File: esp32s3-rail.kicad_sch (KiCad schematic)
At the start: 42 parts, among them J1 RJ45_Wuerth_7499010121A, J2 WR-WST 490107670412, Q1 AO3407A, U1 ESP32-S3-MINI-1U, U2 W5500, U3 THVD1420D, Y1 25M

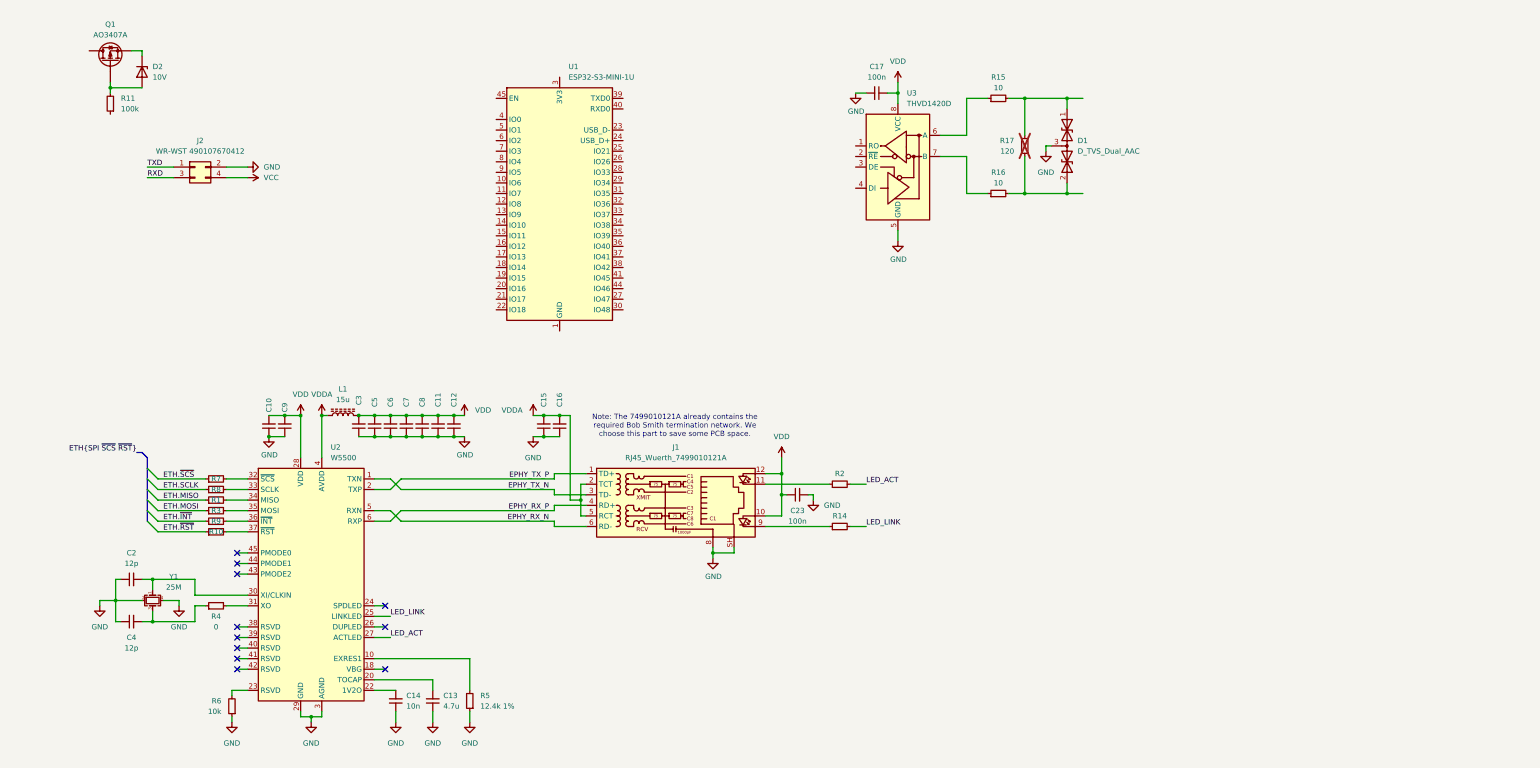
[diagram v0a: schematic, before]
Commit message: Update schematic: - Add RS485 ports - Add USB ports - Add 24V I/O ports
Signed-off-by: Dominik Bayerl <dominik.bayerl@carissma.eu>
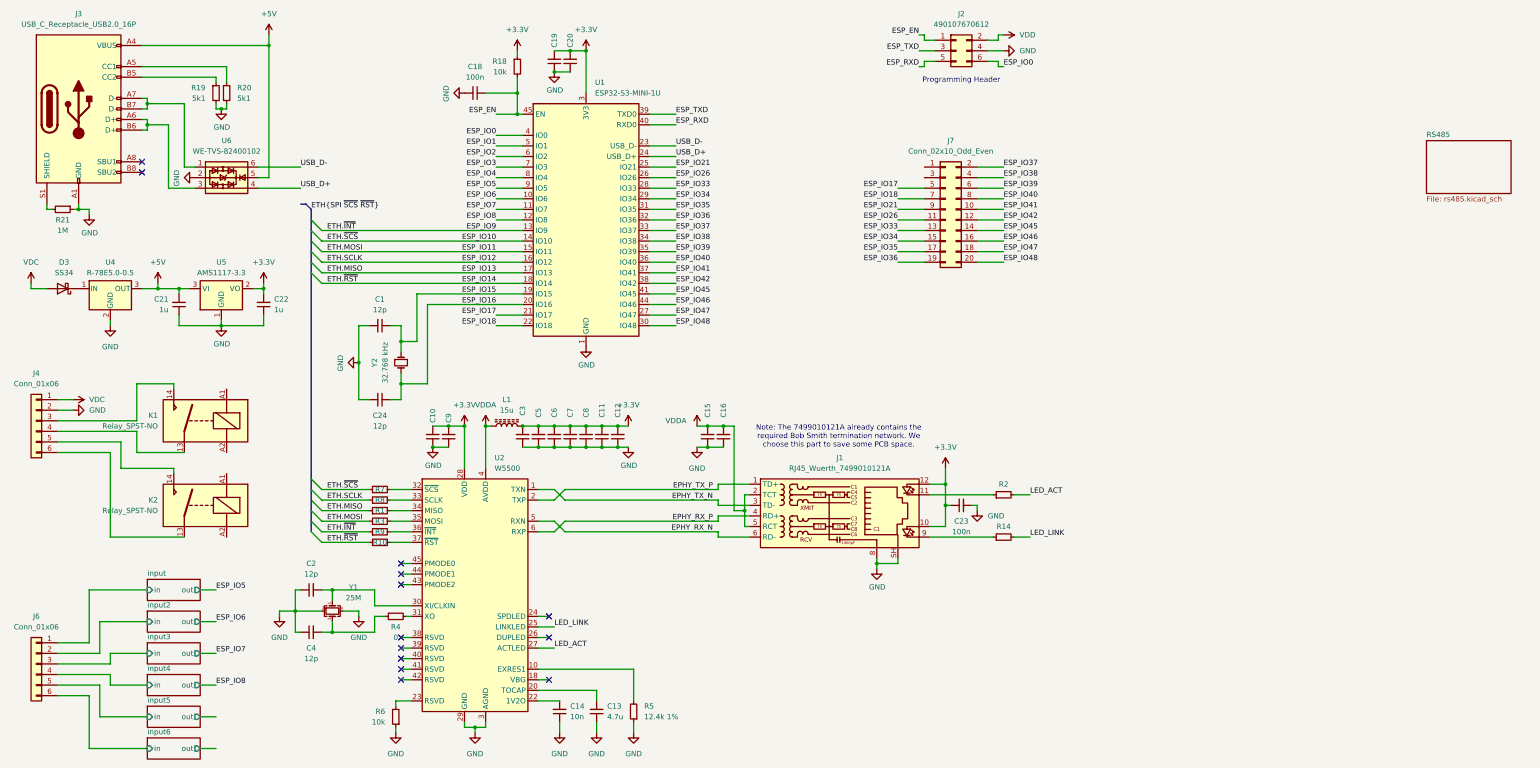
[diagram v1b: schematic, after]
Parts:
- removed C17: 100n, symbol Device:C_Small
- removed D1: D_TVS_Dual_AAC, Package_TO_SOT_SMD:SOT-23, symbol Device:D_TVS_Dual_AAC
- removed D2: 10V, symbol Device:D_Zener
- removed J2: WR-WST 490107670412, Connector_Wuerth_WST:Würth_WR-WST_debug_490107670412_2x02_P2.54mm_Vertical, symbol Connector_Generic:Conn_02x02_Odd_Even
- removed Q1: AO3407A, Package_TO_SOT_SMD:SOT-23, symbol Device:Q_PMOS
- removed R11: 100k, Resistor_SMD:R_0603_1608Metric, symbol Device:R_Small
- removed R15, R16: 10, Resistor_SMD:R_1206_3216Metric, symbol Device:R_Small
- removed R17: 120, Resistor_SMD:R_1206_3216Metric, symbol Device:R_Small
- removed U3: THVD1420D, Package_SO:SOIC-8_3.9x4.9mm_P1.27mm, symbol Interface_UART:THVD1420D
- added C1, C24: 12p, symbol Device:C_Small
- added C18: 100n, symbol Device:C_Small
- added C19, C20, C21, C22: 1u, symbol Device:C_Small
- added D3: SS34, symbol Device:D_Schottky
- added J2: 490107670612, Connector_Wuerth_WST:Würth_WR-WST_debug_490107670612_2x03_P2.54mm_Vertical, symbol Connector_Generic:Conn_02x03_Odd_Even
- added J3: USB_C_Receptacle_USB2.0_16P, symbol Connector:USB_C_Receptacle_USB2.0_16P
- added J4, J6: Conn_01x06, symbol Connector_Generic:Conn_01x06
- added J7: Conn_02x10_Odd_Even, symbol Connector_Generic:Conn_02x10_Odd_Even
- added K1, K2: Relay_SPST-NO, symbol Relay:Relay_SPST-NO
- added R18: 10k, Resistor_SMD:R_1206_3216Metric, symbol Device:R_Small
- added R19, R20: 5k1, Resistor_SMD:R_1206_3216Metric, symbol Device:R_Small
- added R21: 1M, Resistor_SMD:R_1206_3216Metric, symbol Device:R_Small
- added U4: R-78E5.0-0.5, Converter_DCDC:Converter_DCDC_RECOM_R-78E-0.5_THT, symbol Regulator_Switching:R-78E5.0-0.5
- added U5: AMS1117-3.3, Package_TO_SOT_SMD:SOT-223-3_TabPin2, symbol Regulator_Linear:AMS1117-3.3
- added U6: WE-TVS-82400102, Package_TO_SOT_SMD:SOT-23-6, symbol Power_Protection:WE-TVS-82400102
- added Y2: 32.768 kHz, Crystal:Crystal_SMD_EuroQuartz_EQ161-2Pin_3.2x1.5mm_HandSoldering, symbol Device:Crystal_Small
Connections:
- net ETH.MISO is gone; now on net ESP_IO13: R1.1
- net ETH.MOSI is gone; now on net ESP_IO11: R3.1
- net ETH.SCLK is gone; now on net ESP_IO12: R8.1
- net ETH.~{INT} is gone; now on net ESP_IO9: R9.1
- net ETH.~{RST} is gone; now on net ESP_IO14: R10.1
- net ETH.~{SCS} is gone; now on net ESP_IO10: R7.1
- net GND: now also U1.1 (GND), U1.2 (GND), U1.42 (GND), U1.43 (GND), U1.46 (GND), U1.47 (GND), U1.48 (GND), U1.49 (GND), U1.50 (GND), U1.51 (GND), U1.52 (GND), U1.53 (GND), U1.54 (GND), U1.55 (GND), U1.56 (GND), U1.57 (GND), U1.58 (GND), U1.59 (GND), U1.60 (GND), U1.61 (GND), U1.62 (GND), U1.63 (GND), U1.64 (GND), U1.65 (GND), C1.2, C18.2, C19.1, C20.1, C21.1, C22.1, C24.2, J2.4 (Pin_4), J3.A1 (GND), J3.A12 (GND), J3.B1 (GND), J3.B12 (GND), J4.2 (Pin_2), R19.2, R20.2, R21.1, U4.2 (GND), U5.1 (GND), U6.2
- net VDD: now also J2.2 (Pin_2); no longer C10.2, C11.2, C12.2, C23.1, C3.2, C5.2, C6.2, C7.2, C8.2, C9.2, J1.10, J1.12, L1.2, U2.28 (VDD)
- net ESP_IO6: now reaches U1.10 (IO6)
- net ESP_IO7: now reaches U1.11 (IO7)
- net ESP_IO8: now reaches U1.12 (IO8)
- net ESP_IO9: now reaches U1.13 (IO9)
- net ESP_IO10: now reaches U1.14 (IO10)
- net ESP_IO11: now reaches U1.15 (IO11)
- net ESP_IO12: now reaches U1.16 (IO12)
- net ESP_IO13: now reaches U1.17 (IO13)
- net ESP_IO14: now reaches U1.18 (IO14)
- net ESP_IO15: now reaches U1.19 (IO15)
- net ESP_IO15: now also C1.1, Y2.1
- net ESP_IO16: now reaches U1.20 (IO16)
- net ESP_IO16: now also C24.1, Y2.2
- net ESP_IO17: now reaches U1.21 (IO17)
- net ESP_IO17: now also J7.5 (Pin_5)
- net ESP_IO18: now reaches U1.22 (IO18)
- net ESP_IO18: now also J7.7 (Pin_7)
- net USB_D-: now reaches U1.23 (USB_D-)
- net USB_D-: now also U6.6
- net USB_D+: now reaches U1.24 (USB_D+)
- net USB_D+: now also U6.4
- net ESP_IO21: now reaches U1.25 (IO21)
- net ESP_IO21: now also J7.9 (Pin_9)
- net ESP_IO26: now reaches U1.26 (IO26)
- net ESP_IO26: now also J7.11 (Pin_11)
- net ESP_IO47: now reaches U1.27 (IO47)
- net ESP_IO47: now also J7.18 (Pin_18)
- net ESP_IO33: now reaches U1.28 (IO33)
- net ESP_IO33: now also J7.13 (Pin_13)
- net ESP_IO34: now reaches U1.29 (IO34)
- net ESP_IO34: now also J7.15 (Pin_15)
- net +3.3V: now reaches U1.3 (3V3)
- net +3.3V: now also C10.2, C11.2, C12.2, C23.1, C3.2, C5.2, C6.2, C7.2, C8.2, C9.2, J1.10, J1.12, L1.2, U2.28 (VDD), C19.2, C20.2, C22.2, R18.1, U5.2 (VO)
- net ESP_IO48: now reaches U1.30 (IO48)
- net ESP_IO48: now also J7.20 (Pin_20)
- net ESP_IO35: now reaches U1.31 (IO35)
- net ESP_IO35: now also J7.17 (Pin_17)
- net ESP_IO36: now reaches U1.32 (IO36)
- net ESP_IO36: now also J7.19 (Pin_19)
- net ESP_IO37: now reaches U1.33 (IO37)
- net ESP_IO37: now also J7.2 (Pin_2)
- net ESP_IO38: now reaches U1.34 (IO38)
- net ESP_IO38: now also J7.4 (Pin_4)
- net ESP_IO39: now reaches U1.35 (IO39)
- net ESP_IO39: now also J7.6 (Pin_6)
- net ESP_IO40: now reaches U1.36 (IO40)
- net ESP_IO40: now also J7.8 (Pin_8)
- net ESP_IO41: now reaches U1.37 (IO41)
- net ESP_IO41: now also J7.10 (Pin_10)
- net ESP_IO42: now reaches U1.38 (IO42)
- net ESP_IO42: now also J7.12 (Pin_12)
- net ESP_TXD: now reaches U1.39 (TXD0)
- net ESP_TXD: now also J2.3 (Pin_3)
- net ESP_IO0: now reaches U1.4 (IO0)
- net ESP_IO0: now also J2.6 (Pin_6)
- net ESP_RXD: now reaches U1.40 (RXD0)
- net ESP_RXD: now also J2.5 (Pin_5)
- net ESP_IO45: now reaches U1.41 (IO45)
- net ESP_IO45: now also J7.14 (Pin_14)
- net ESP_IO46: now reaches U1.44 (IO46)
- net ESP_IO46: now also J7.16 (Pin_16)
- net ESP_EN: now reaches U1.45 (EN)
- net ESP_EN: now also C18.1, J2.1 (Pin_1), R18.2
- net ESP_IO1: now reaches U1.5 (IO1)
- net ESP_IO2: now reaches U1.6 (IO2)
- net ESP_IO3: now reaches U1.7 (IO3)
- net ESP_IO4: now reaches U1.8 (IO4)
- net ESP_IO5: now reaches U1.9 (IO5)
- new net: J4.4 (Pin_4), K1.13
- new net: J4.3 (Pin_3), K1.14
- new net: J3.A5 (CC1), R20.1
- new net: J3.A7 (D-), J3.B7 (D-), U6.1
- new net: J3.A6 (D+), J3.B6 (D+), U6.3
- new net: J3.B5 (CC2), R19.1
- new net: J3.S1 (SHIELD), R21.2
- new net: D3.1 (K), U4.1 (IN)
- new net: J4.6 (Pin_6), K2.13
- new net: J4.5 (Pin_5), K2.14
- new net +5V: C21.2, J3.A4 (VBUS), J3.A9 (VBUS), J3.B4 (VBUS), J3.B9 (VBUS), U4.3 (OUT), U5.3 (VI), U6.5
- new net VDC: D3.2 (A), J4.1 (Pin_1)
- new net input/in: J6.1 (Pin_1)
- new net input2/in: J6.2 (Pin_2)
- new net input3/in: J6.3 (Pin_3)
- new net input4/in: J6.4 (Pin_4)
- new net input5/in: J6.5 (Pin_5)
- new net input6/in: J6.6 (Pin_6)
- no-connect marks 11 -> 13
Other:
- added sheet RS485 (rs485.kicad_sch)
- added sheet input (input.kicad_sch)
- added sheet input2 (input.kicad_sch)
- added sheet input3 (input.kicad_sch)
- added sheet input4 (input.kicad_sch)
- added sheet input5 (input.kicad_sch)
- added sheet input6 (input.kicad_sch)
- note added: "Programming Header"
- moved on the sheet: C10, C11, C12, C13, C14, C15, C16, C2, C23, C3, C4, C5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

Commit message: Finish rev0 schematics.
Signed-off-by: Dominik Bayerl <dominik.bayerl@carissma.eu>
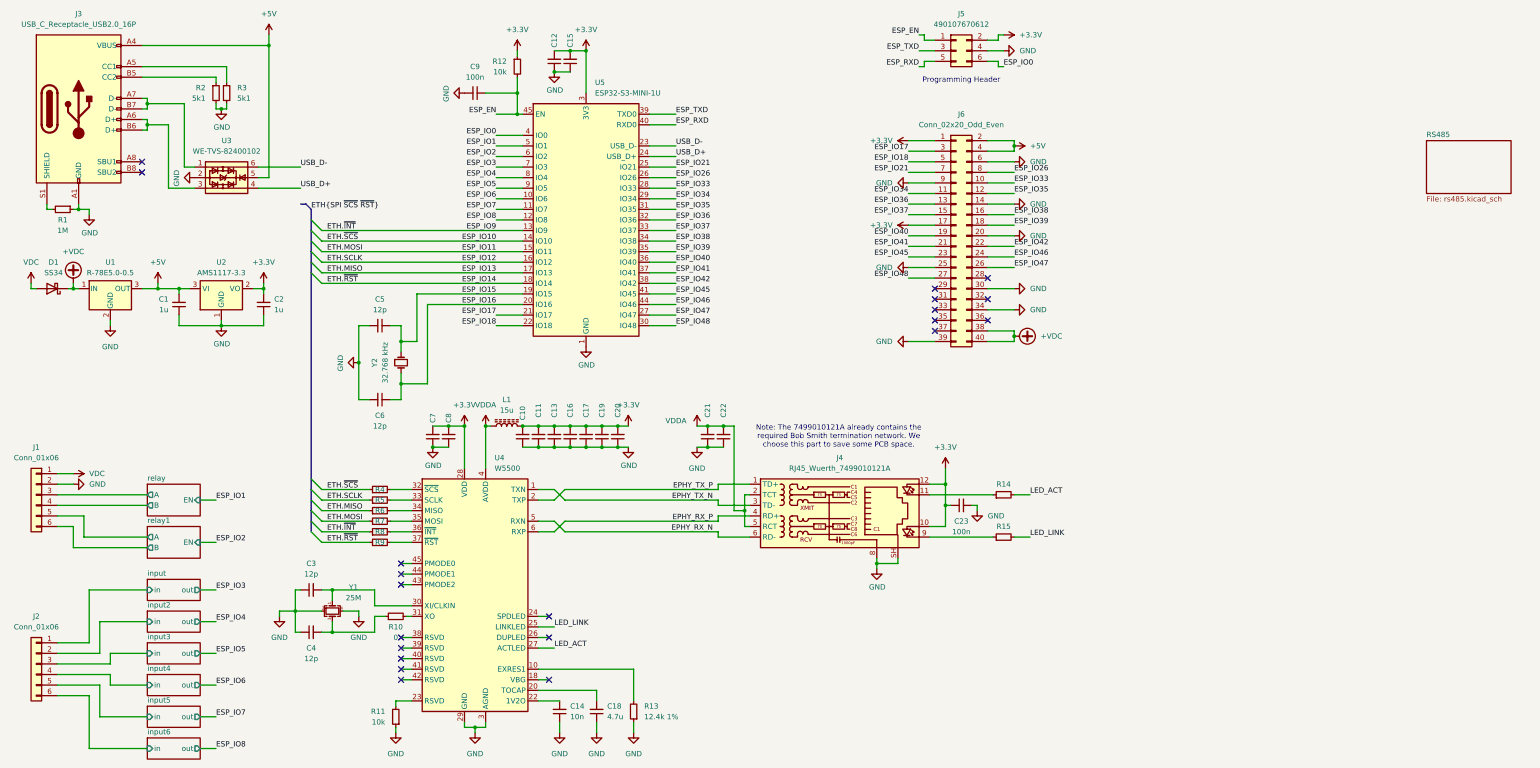
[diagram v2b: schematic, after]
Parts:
- removed K1, K2: Relay_SPST-NO, symbol Relay:Relay_SPST-NO
- C1: renamed from C21; footprint (none) -> Capacitor_SMD:C_0603_1608Metric_Pad1.08x0.95mm_HandSolder
- C10: renamed from C3; footprint (none) -> Capacitor_SMD:C_0603_1608Metric_Pad1.08x0.95mm_HandSolder
- C11: renamed from C5; footprint (none) -> Capacitor_SMD:C_0603_1608Metric_Pad1.08x0.95mm_HandSolder
- C12: renamed from C19; footprint (none) -> Capacitor_SMD:C_0603_1608Metric_Pad1.08x0.95mm_HandSolder
- C13: renamed from C6; footprint (none) -> Capacitor_SMD:C_0603_1608Metric_Pad1.08x0.95mm_HandSolder
- C14, C4: footprint (none) -> Capacitor_SMD:C_0603_1608Metric_Pad1.08x0.95mm_HandSolder
- C15: renamed from C20; footprint (none) -> Capacitor_SMD:C_0603_1608Metric_Pad1.08x0.95mm_HandSolder
- C16: renamed from C7; footprint (none) -> Capacitor_SMD:C_0603_1608Metric_Pad1.08x0.95mm_HandSolder
- C17: renamed from C8; footprint (none) -> Capacitor_SMD:C_0603_1608Metric_Pad1.08x0.95mm_HandSolder
- C18: renamed from C13; footprint (none) -> Capacitor_SMD:C_0603_1608Metric_Pad1.08x0.95mm_HandSolder
- C19: renamed from C11; footprint (none) -> Capacitor_SMD:C_0603_1608Metric_Pad1.08x0.95mm_HandSolder
- C2: renamed from C22; footprint (none) -> Capacitor_SMD:C_0603_1608Metric_Pad1.08x0.95mm_HandSolder
- C20: renamed from C12; footprint (none) -> Capacitor_SMD:C_0603_1608Metric_Pad1.08x0.95mm_HandSolder
- C21: renamed from C15; footprint (none) -> Capacitor_SMD:C_0603_1608Metric_Pad1.08x0.95mm_HandSolder
- C22: renamed from C16; footprint (none) -> Capacitor_SMD:C_0603_1608Metric_Pad1.08x0.95mm_HandSolder
- C23: footprint Capacitor_SMD:C_0603_1608Metric -> Capacitor_SMD:C_0603_1608Metric_Pad1.08x0.95mm_HandSolder
- C3: renamed from C2; footprint (none) -> Capacitor_SMD:C_0603_1608Metric_Pad1.08x0.95mm_HandSolder
- C5: renamed from C1; footprint (none) -> Capacitor_SMD:C_0603_1608Metric_Pad1.08x0.95mm_HandSolder
- C6: renamed from C24; footprint (none) -> Capacitor_SMD:C_0603_1608Metric_Pad1.08x0.95mm_HandSolder
- C7: renamed from C10; footprint (none) -> Capacitor_SMD:C_0603_1608Metric_Pad1.08x0.95mm_HandSolder
- C8: renamed from C9; footprint (none) -> Capacitor_SMD:C_0603_1608Metric_Pad1.08x0.95mm_HandSolder
- C9: renamed from C18; footprint (none) -> Capacitor_SMD:C_0603_1608Metric_Pad1.08x0.95mm_HandSolder
- D1: renamed from D3; footprint (none) -> Diode_SMD:D_SMC_Handsoldering
- J3: footprint (none) -> Connector_USB:USB_C_Receptacle_HRO_TYPE-C-31-M-12
- J6: renamed from J7; value Conn_02x10_Odd_Even -> Conn_02x20_Odd_Even; footprint (none) -> Connector_PinSocket_2.54mm:PinSocket_2x20_P2.54mm_Vertical; symbol Connector_Generic:Conn_02x10_Odd_Even -> Connector_Generic:Conn_02x20_Odd_Even
- L1: footprint (none) -> Inductor_SMD:L_0603_1608Metric_Pad1.05x0.95mm_HandSolder
- renumbered J4 to J1, J6 to J2, J1 to J4, J2 to J5, R21 to R1, R4 to R10, R6 to R11, R18 to R12, R5 to R13, R2 to R14, R14 to R15, R19 to R2, R20 to R3, R7 to R4, R8 to R5, R1 to R6, R3 to R7, R9 to R8, R10 to R9, U4 to U1, U5 to U2, U6 to U3, U2 to U4, U1 to U5
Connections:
- net VDD is gone; now on net +3.3V: J5.2 (Pin_2)
- net +3.3V: now also J6.1 (Pin_1), J6.17 (Pin_17)
- net +5V: now also J6.2 (Pin_2), J6.4 (Pin_4)
- net ESP_IO17: now also J6.3 (Pin_3); no longer J6.5 (Pin_5)
- net ESP_IO18: now also J6.5 (Pin_5); no longer J6.7 (Pin_7)
- net ESP_IO21: now also J6.7 (Pin_7); no longer J6.9 (Pin_9)
- net ESP_IO26: now also J6.8 (Pin_8); no longer J6.11 (Pin_11)
- net ESP_IO33: now also J6.10 (Pin_10); no longer J6.13 (Pin_13)
- net ESP_IO34: now also J6.11 (Pin_11); no longer J6.15 (Pin_15)
- net ESP_IO35: now also J6.12 (Pin_12); no longer J6.17 (Pin_17)
- net ESP_IO36: now also J6.13 (Pin_13); no longer J6.19 (Pin_19)
- net ESP_IO37: now also J6.15 (Pin_15); no longer J6.2 (Pin_2)
- net ESP_IO38: now also J6.16 (Pin_16); no longer J6.4 (Pin_4)
- net ESP_IO39: now also J6.18 (Pin_18); no longer J6.6 (Pin_6)
- net ESP_IO40: now also J6.19 (Pin_19); no longer J6.8 (Pin_8)
- net ESP_IO41: now also J6.21 (Pin_21); no longer J6.10 (Pin_10)
- net ESP_IO42: now also J6.22 (Pin_22); no longer J6.12 (Pin_12)
- net ESP_IO45: now also J6.23 (Pin_23); no longer J6.14 (Pin_14)
- net ESP_IO46: now also J6.24 (Pin_24); no longer J6.16 (Pin_16)
- net ESP_IO47: now also J6.26 (Pin_26); no longer J6.18 (Pin_18)
- net ESP_IO48: now also J6.27 (Pin_27); no longer J6.20 (Pin_20)
- net GND: now also J6.14 (Pin_14), J6.20 (Pin_20), J6.25 (Pin_25), J6.30 (Pin_30), J6.34 (Pin_34), J6.39 (Pin_39), J6.6 (Pin_6), J6.9 (Pin_9)
- net relay/B: now reaches J1.4 (Pin_4)
- net relay/A: now reaches J1.3 (Pin_3)
- net +VDC: now reaches D1.1 (K), U1.1 (IN)
- net +VDC: now also J6.38 (Pin_38), J6.40 (Pin_40)
- net relay1/B: now reaches J1.6 (Pin_6)
- net relay1/A: now reaches J1.5 (Pin_5)
- no-connect marks 13 -> 21
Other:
- added sheet relay (relay.kicad_sch)
- added sheet relay1 (relay.kicad_sch)
- moved on the sheet: D1, J1
